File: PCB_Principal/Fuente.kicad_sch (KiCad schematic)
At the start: 27 parts, among them J1 Vin, U2 LM350_TO3, U3 LM350_TO3, U4 LM337_TO220, U5 TL431LP, U6 LM117_TO3

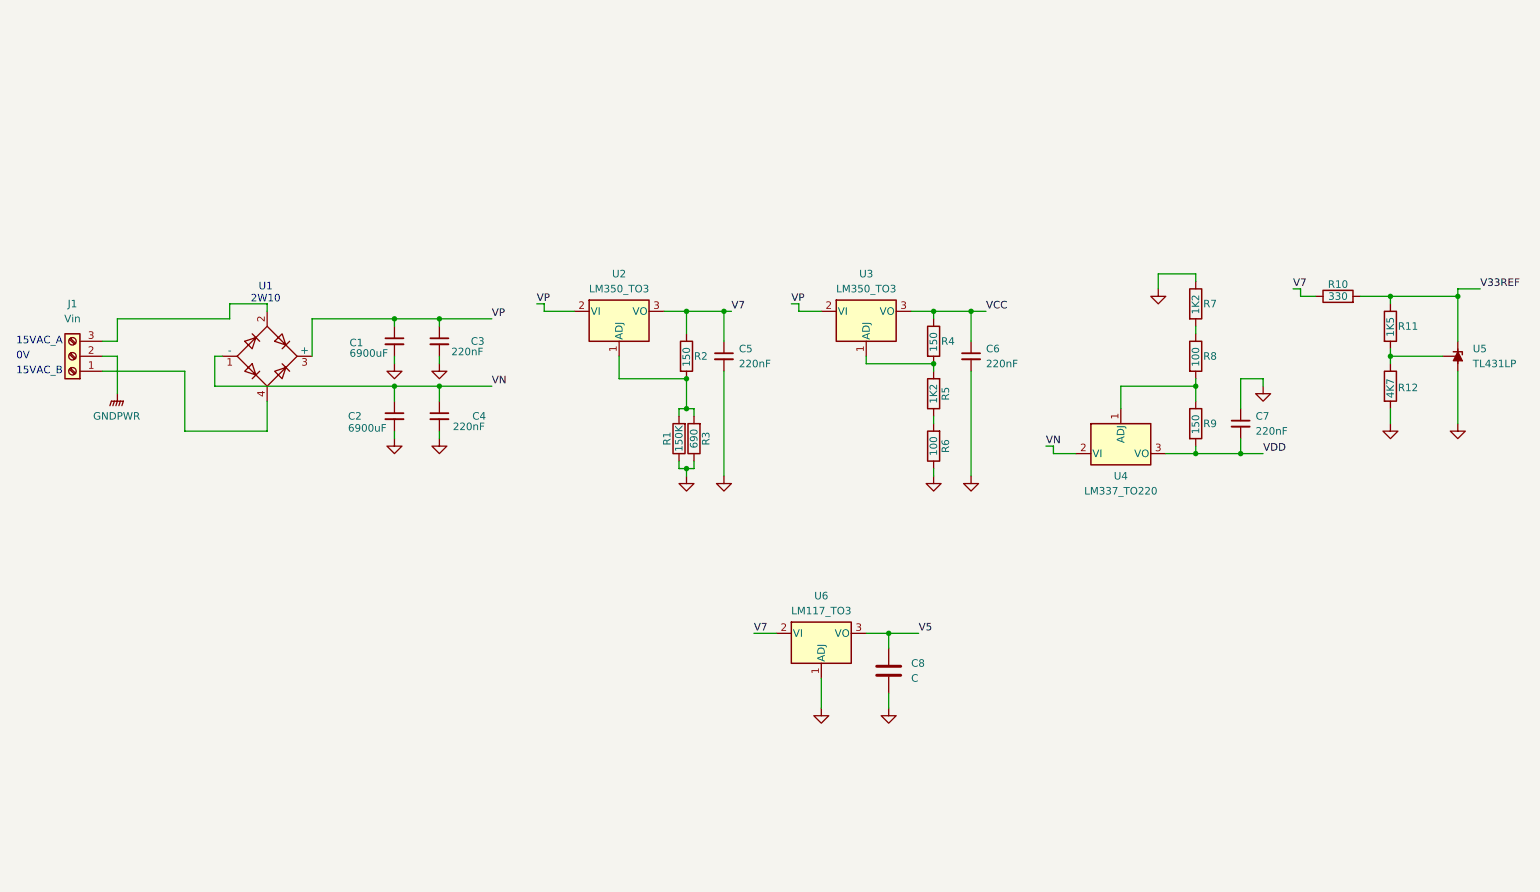
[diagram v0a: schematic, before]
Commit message: Versión 2 de esquemático, por GC.
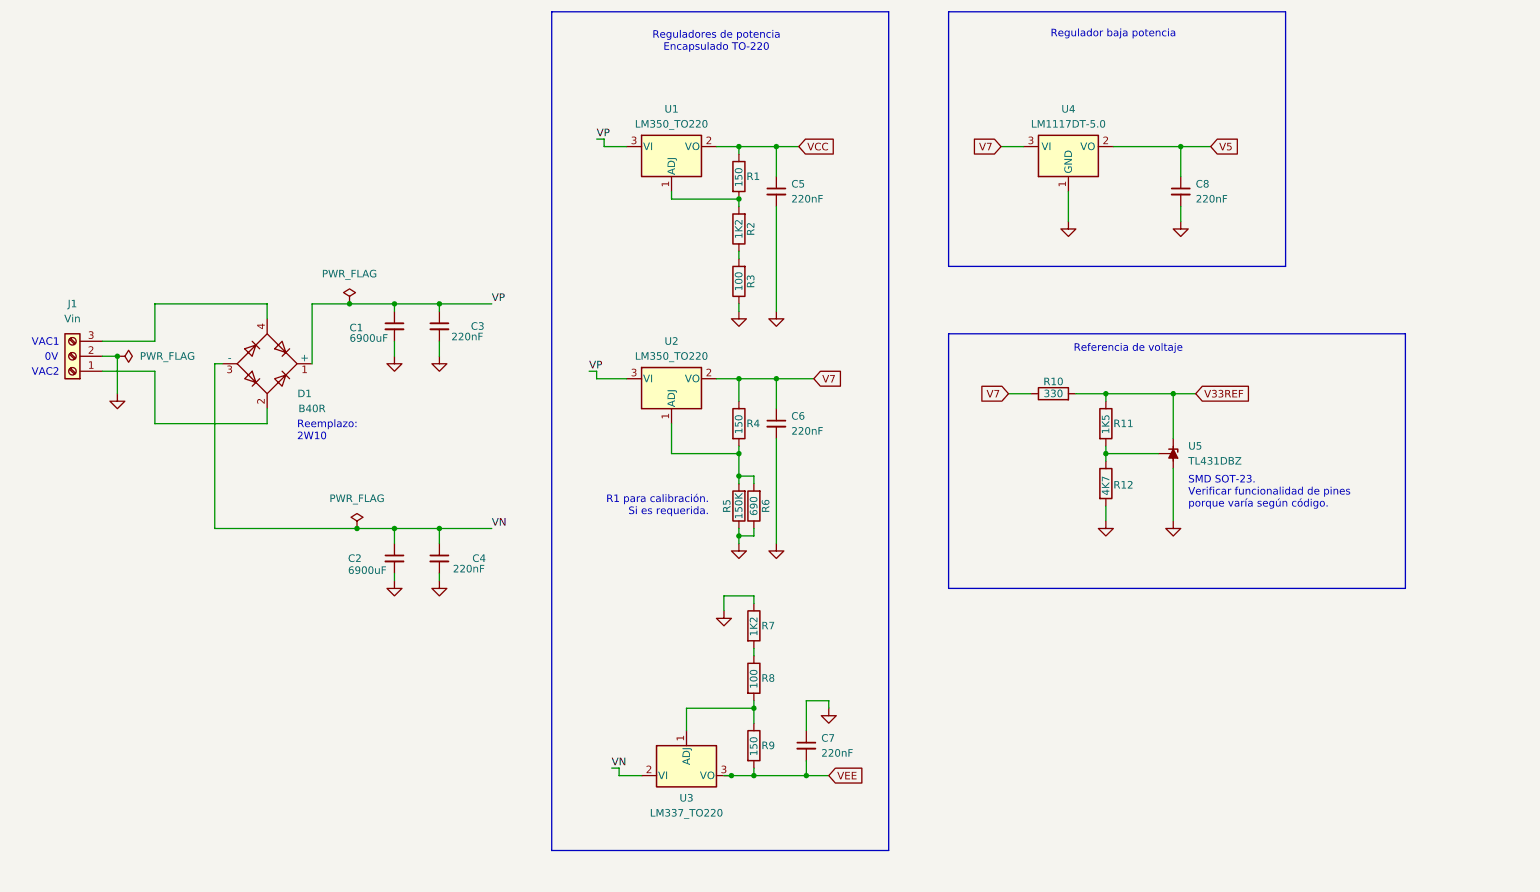
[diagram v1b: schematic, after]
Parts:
- removed C8: C, symbol Device:C
- removed D10: B40C2300-1500B, Diode_THT:Diode_Bridge_19.0x3.5x10.0mm_P5.0mm, symbol Diode_Bridge:B40C2300-1500B
- removed U2, U3: LM350_TO3, Package_TO_SOT_THT:TO-3, symbol Regulator_Linear:LM350_TO3
- removed U5: TL431LP, Package_TO_SOT_THT:TO-92_Inline, symbol Reference_Voltage:TL431LP
- removed U6: LM117_TO3, Package_TO_SOT_THT:TO-3, symbol Regulator_Linear:LM117_TO3
- added C8: 220nF, Capacitor_SMD:C_1206_3216Metric_Pad1.33x1.80mm_HandSolder, symbol Device:C_Small
- added D1: B40R, Diode_THT:Diode_Bridge_Round_D9.0mm, symbol Diode_Bridge:B40R
- added U1, U2: LM350_TO220, Package_TO_SOT_THT:TO-220-3_Vertical, symbol Regulator_Linear:LM350_TO220
- added U4: LM1117DT-5.0, Package_TO_SOT_SMD:TO-252-3_TabPin2, symbol Regulator_Linear:LM1117DT-5.0
- added U5: TL431DBZ, Package_TO_SOT_SMD:SOT-23, symbol Reference_Voltage:TL431DBZ
- C1, C2: footprint (none) -> Capacitor_THT:CP_Radial_D18.0mm_P7.50mm
- C3, C4, C7: footprint (none) -> Capacitor_SMD:C_1206_3216Metric_Pad1.33x1.80mm_HandSolder
- C5: renamed from C6; footprint (none) -> Capacitor_SMD:C_1206_3216Metric_Pad1.33x1.80mm_HandSolder
- C6: renamed from C5; footprint (none) -> Capacitor_SMD:C_1206_3216Metric_Pad1.33x1.80mm_HandSolder
- J1: footprint (none) -> TerminalBlock_Phoenix:TerminalBlock_Phoenix_MKDS-1,5-3-5.08_1x03_P5.08mm_Horizontal
- R1: renamed from R4; footprint (none) -> Resistor_SMD:R_1206_3216Metric_Pad1.30x1.75mm_HandSolder
- R10, R11, R12, R7, R8, R9: footprint (none) -> Resistor_SMD:R_1206_3216Metric_Pad1.30x1.75mm_HandSolder
- R2: renamed from R5; footprint (none) -> Resistor_SMD:R_1206_3216Metric_Pad1.30x1.75mm_HandSolder
- R3: renamed from R6; footprint (none) -> Resistor_SMD:R_1206_3216Metric_Pad1.30x1.75mm_HandSolder
- R4: renamed from R2; footprint (none) -> Resistor_SMD:R_1206_3216Metric_Pad1.30x1.75mm_HandSolder
- R5: renamed from R1; footprint (none) -> Resistor_SMD:R_1206_3216Metric_Pad1.30x1.75mm_HandSolder
- R6: renamed from R3; footprint (none) -> Resistor_SMD:R_1206_3216Metric_Pad1.30x1.75mm_HandSolder
- renumbered U4 to U3
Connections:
- net GNDPWR is gone; now on net GND: J1.2 (Pin_2)
- net GND: now also C8.2, U4.1 (GND), U5.3 (A)
- net V33REF: now also U5.1 (K)
- net V5: now also C8.1, U4.2 (VO)
- net V7: now also U2.2 (VO), U4.3 (VI)
- net VCC: now also U1.2 (VO)
- net VN: now also D1.3 (-)
- net VP: now also D1.1 (+), U1.3 (VI), U2.3 (VI)
- net at R4.2, R5.2, R6.2: now also U2.1 (ADJ)
- net at R11.2, R12.1: now also U5.2 (REF)
- net at R1.2, R2.2: now also U1.1 (ADJ)
- net at J1.3 (Pin_3): now also D1.4
- net at J1.1 (Pin_1): now also D1.2
- net VDD renamed VEE
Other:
- note added: "R1 para calibración. Si es requerida."
- note added: "Reemplazo: 2W10"
- note added: "Referencia de voltaje"
- note added: "Regulador baja potencia"
- note added: "Reguladores de potencia Encapsulado TO-220"
- note added: "SMD SOT-23. Verificar funcionalidad de pines porque varía según código."
- note added: "VAC1"
- note added: "VAC2"
- note removed: "15VAC_A"
- note removed: "15VAC_B"
- note removed: "U1 2W10"
- company: (none) -> UNDAV
- title: (none) -> Fuente (ISPEL Beta 2024)
- moved on the sheet: C1, C2, C3, C4, C5, C6, C7, R1, R10, R11, R12, R2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

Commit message: Iniciando PCB...
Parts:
- removed J1: Vin, TerminalBlock_Phoenix:TerminalBlock_Phoenix_MKDS-1,5-3-5.08_1x03_P5.08mm_Horizontal, symbol Connector:Screw_Terminal_01x03
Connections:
- net GND: now also C2.1; no longer C2.2
- net VN: now also C2.2; no longer C2.1
- net VAC2: now reaches D1.2
- net VAC1: now reaches D1.4
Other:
- note removed: "0V"
- note removed: "VAC1"
- note removed: "VAC2"
- moved on the sheet: C2, R10, R11, R12, U5

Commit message: Versión 1 - ISPEL Beta 2024 para fabricar.
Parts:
- added RT1, RT2, RT3, RT4, RT5: 1, Resistor_SMD:R_1206_3216Metric_Pad1.30x1.75mm_HandSolder, symbol Device:R
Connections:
- net V5: now also RT3.1, RT3.2
- net VCC: now also RT1.1, RT1.2, RT4.1, RT4.2
- net VEE: now also RT2.1, RT2.2, RT5.1, RT5.2
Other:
- note added: "Resistencias para test"
- moved on the sheet: C1, C2, C3, C4, C5, C6, C7, C8, D1, R1, R10, R11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

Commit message: Revisión 1. Con prototipo ISPEL Beta 2024 en fase de prueba.
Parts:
- C5, C6, C7, C8: value 220nF -> 1uF
- RT1, RT2, RT3, RT4, RT5: value 1 -> 0.1
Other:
- title: Fuente (ISPEL Beta 2024) -> Fuente (ISPEL Beta)
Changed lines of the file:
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@@
 	(paper "A4")
 	(title_block
-		(title "Fuente (ISPEL Beta 2024)")
-		(date "2024-10-29")
-		(rev "2 (GC)")
+		(title "Fuente (ISPEL Beta)")
+		(date "2025-04-04")
+		(rev "1")
 		(company "UNDAV")
 	)
@@
 			)
 		)
-		(property "Value" "1"
+		(property "Value" "0.1"
 			(at 242.57 147.828 90)
 			(effects
@@
 			)
 		)
-		(property "Value" "1"
+		(property "Value" "0.1"
 			(at 222.25 147.828 90)
 			(effects
@@
 			)
 		)
-		(property "Value" "220nF"
+		(property "Value" "1uF"
 			(at 148.59 57.1562 0)
 			(effects
@@
 			)
 		)
-		(property "Value" "220nF"
+		(property "Value" "1uF"
 			(at 219.71 50.8062 0)
 			(effects
@@
 			)
 		)
-		(property "Value" "220nF"
+		(property "Value" "1uF"
 			(at 148.59 96.5262 0)
 			(effects
@@
 			)
 		)
-		(property "Value" "1"
+		(property "Value" "0.1"
 			(at 214.63 147.828 90)
 			(effects
@@
 			)
 		)
-		(property "Value" "220nF"
+		(property "Value" "1uF"
 			(at 153.67 151.1362 0)
 			(effects
@@
 			)
 		)
-		(property "Value" "1"
+		(property "Value" "0.1"
 			(at 193.04 147.828 90)
 			(effects
@@
 			)
 		)
-		(property "Value" "1"
+		(property "Value" "0.1"
 			(at 186.69 147.828 90)
 			(effects
